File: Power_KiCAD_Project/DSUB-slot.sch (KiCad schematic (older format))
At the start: 2 parts, among them J7 L717SDC37P1ACH4F

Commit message: updated pcb
more updates because stuff was a bit too far away from their connected components
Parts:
- J7: footprint Connector_Dsub:DSUB-37_Male_Horizontal_P2.77x2.84mm_EdgePinOffset9.90mm_Housed_MountingHolesOffset11.32mm -> SamacSys_Parts:L717SDC37P1ACH4F
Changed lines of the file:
@@
 F 0 "J7" V 6019 1600 50  0000 C CNN
 F 1 "L717SDC37P1ACH4F" V 6110 1600 50  0000 C CNN
-F 2 "Connector_Dsub:DSUB-37_Male_Horizontal_P2.77x2.84mm_EdgePinOffset9.90mm_Housed_MountingHolesOffset11.32mm" H 8450 1900 50  0001 L CNN
+F 2 "SamacSys_Parts:L717SDC37P1ACH4F" H 8450 1900 50  0001 L CNN
 F 3 "https://cdn.amphenol-icc.com/media/wysiwyg/files/drawing/l717sdxxxp1ach4f.pdf" H 8450 1800 50  0001 L CNN
 F 4 "D-Sub Standard Connectors 37P Sz C Std Density Pin Screwlock 4-40" H 8450 1700 50  0001 L CNN "Description"

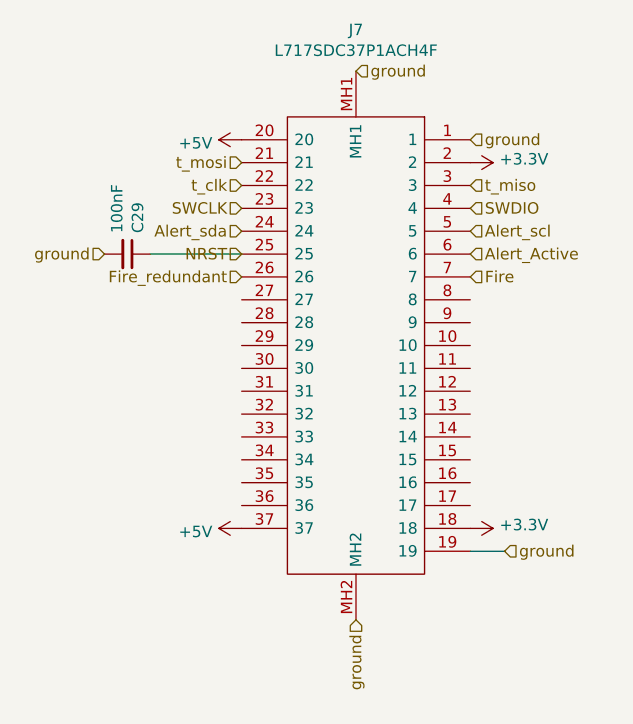
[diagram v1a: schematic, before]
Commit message: Changes to PCB
re did the pcb and added a "switch"
basically its just an xt60 connector in series with the other ones that needs to be shorted for the board to get power
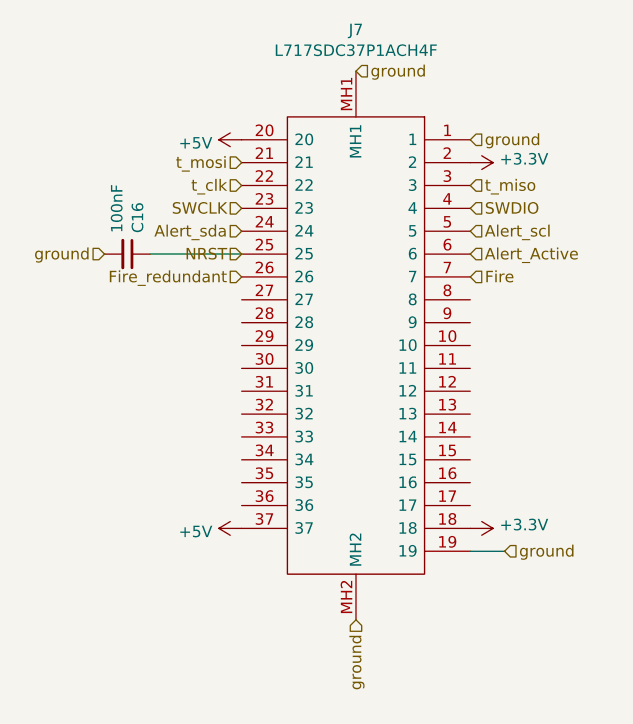
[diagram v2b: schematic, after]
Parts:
- renumbered C29 to C16
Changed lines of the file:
@@
 AR Path="/61A55586" Ref="C?"  Part="1"
 AR Path="/61A437B5/61A55586" Ref="C?"  Part="1"
-AR Path="/61D3585E/61A55586" Ref="C29"  Part="1"
-F 0 "C29" H 5292 2446 50  0000 L CNN
+AR Path="/61D3585E/61A55586" Ref="C16"  Part="1"
+F 0 "C16" H 5292 2446 50  0000 L CNN
 F 1 "100nF" H 5292 2355 50  0000 L CNN
 F 2 "Capacitor_SMD:C_0603_1608Metric" H 5200 2400 50  0001 C CNN
@@
 	5300 2400 5700 2400
 $Comp
-L power:+3.3V #PWR022
+L power:+3.3V #PWR010
 U 1 1 61A4A3FB
 P 6700 2000
-F 0 "#PWR022" H 6700 1850 50  0001 C CNN
+F 0 "#PWR010" H 6700 1850 50  0001 C CNN
 F 1 "+3.3V" V 6715 2128 50  0000 L CNN
 F 2 "" H 6700 2000 50  0001 C CNN
@@
 $EndComp
 $Comp
-L power:+5V #PWR020
+L power:+5V #PWR08
 U 1 1 61A491E6
 P 5700 1900
-F 0 "#PWR020" H 5700 1750 50  0001 C CNN
+F 0 "#PWR08" H 5700 1750 50  0001 C CNN
 F 1 "+5V" V 5715 2028 50  0000 L CNN
 F 2 "" H 5700 1900 50  0001 C CNN
@@
 $EndComp
 $Comp
-L power:+3.3V #PWR023
+L power:+3.3V #PWR011
 U 1 1 61A4AB5D
 P 6700 3600
-F 0 "#PWR023" H 6700 3450 50  0001 C CNN
+F 0 "#PWR011" H 6700 3450 50  0001 C CNN
 F 1 "+3.3V" V 6715 3728 50  0000 L CNN
 F 2 "" H 6700 3600 50  0001 C CNN
@@
 	6850 3700 6700 3700
 $Comp
-L power:+5V #PWR021
+L power:+5V #PWR09
 U 1 1 61A49AB4
 P 5700 3600
-F 0 "#PWR021" H 5700 3450 50  0001 C CNN
+F 0 "#PWR09" H 5700 3450 50  0001 C CNN
 F 1 "+5V" V 5715 3728 50  0000 L CNN
 F 2 "" H 5700 3600 50  0001 C CNN
